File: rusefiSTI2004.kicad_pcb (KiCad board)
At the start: 4 copper layers, 138.6 x 113.6 mm, 137 parts, among them J1 TE_1-1376430-0, J2 USB C 2.0 16P, J3 Molex_39281143, M1 Module-mega-mcu144-0.7, M10 Module-lin-0.1, M11 Module-dinput4-0.1, M12 Module-dinput4-0.1, M13 Module-knock-0.2, M14 Module-power_12and5V-0.3, M2 Module-motor-driver-0.1, M3 Module-wbo-0.5, M5 Module-vr-discrete-0.5, M8 Module-power_12and5V-0.3, M9 Module-motor-driver-0.1, P1 WBO_UN, P10 OUT_SPARE_LS2, P11 CHARGE_A22, P12 FP_STATUS, P13 DLC6_D29, P14 SPARE_IGN6, P15 SPARE_IGN7, P16 SPARE_IGN8, P17 I2C_1_SCL, P18 I2C_1_SDA, P19 +5VA, P2 WBO_VM, P20 +3.3V, P21 +12V_RAW, P22 GND, P23 BOOT0, P24 SWDIO, P25 SWCLK, P26 NRST, P27 SPARE_PWM3, P28 SPARE_RES2, P29 AUX_IN1, P3 WBO_IP, P30 AUX_IN2, P31 AUX_IN3, P32 PG_5VP_APS, P4 WBO_RTRIM, P5 WBO_HEATER, P6 CAN_H, P7 CAN_L, P8 K_LINE, P9 OUT_SPARE_LS1, Q1 NCV8401BDTRKG, Q10 NCV8401BDTRKG, Q11 NCV8401BDTRKG, Q12 NCV8401BDTRKG, Q13 ZXMS6006DGQ-13, Q14 ZXMS6006DGQ-13, Q15 ZXMS6006DGQ-13, Q16 ZXMS6006DGQ-13, Q17 ZXMS6004FFTA, Q18 ZXMS6004FFTA, Q19 ZXMS6004FFTA, Q2 NCV8401BDTRKG, Q20 ZXMS6004FFTA, Q3 NCV8401BDTRKG, Q4 NCV8401BDTRKG, Q5 ZXMS6004FFTA, Q6 ZXMS6004FFTA, Q7 ZXMS6004FFTA, Q8 ZXMS6004FFTA, Q9 NCV8401BDTRKG, U1 USBLC6-2SC6

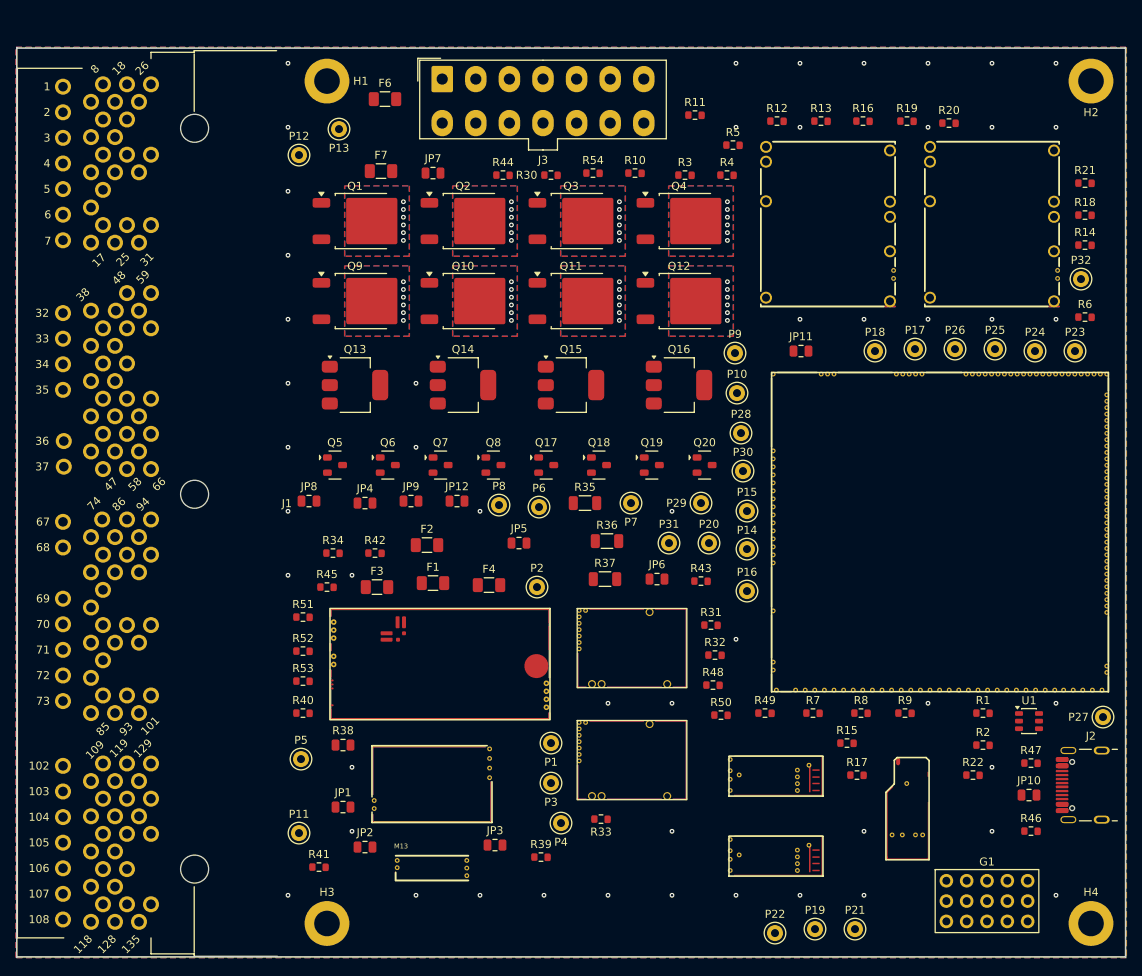
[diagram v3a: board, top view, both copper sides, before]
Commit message: Low-side drivers as on the newest rusEFI boards: 10 x VNLD5160 dual SO-8 + 1 NCV8401B DPAK for the rear O2 heater
rusEFI uaefi-f, hellen-112-17 and hellen154hyundai-e use VNLD5090/VNLD5160 for general outputs and
keep one DPAK for the heaviest load; our Hellen modules already carry their other ICs. Every output
keeps its J1 and MCU pin (netlist checked); U19B parked as a spare. PCB re-placed: DRC 0 errors.

Co-Authored-By: Claude Opus 5.5 <noreply@anthropic.com>
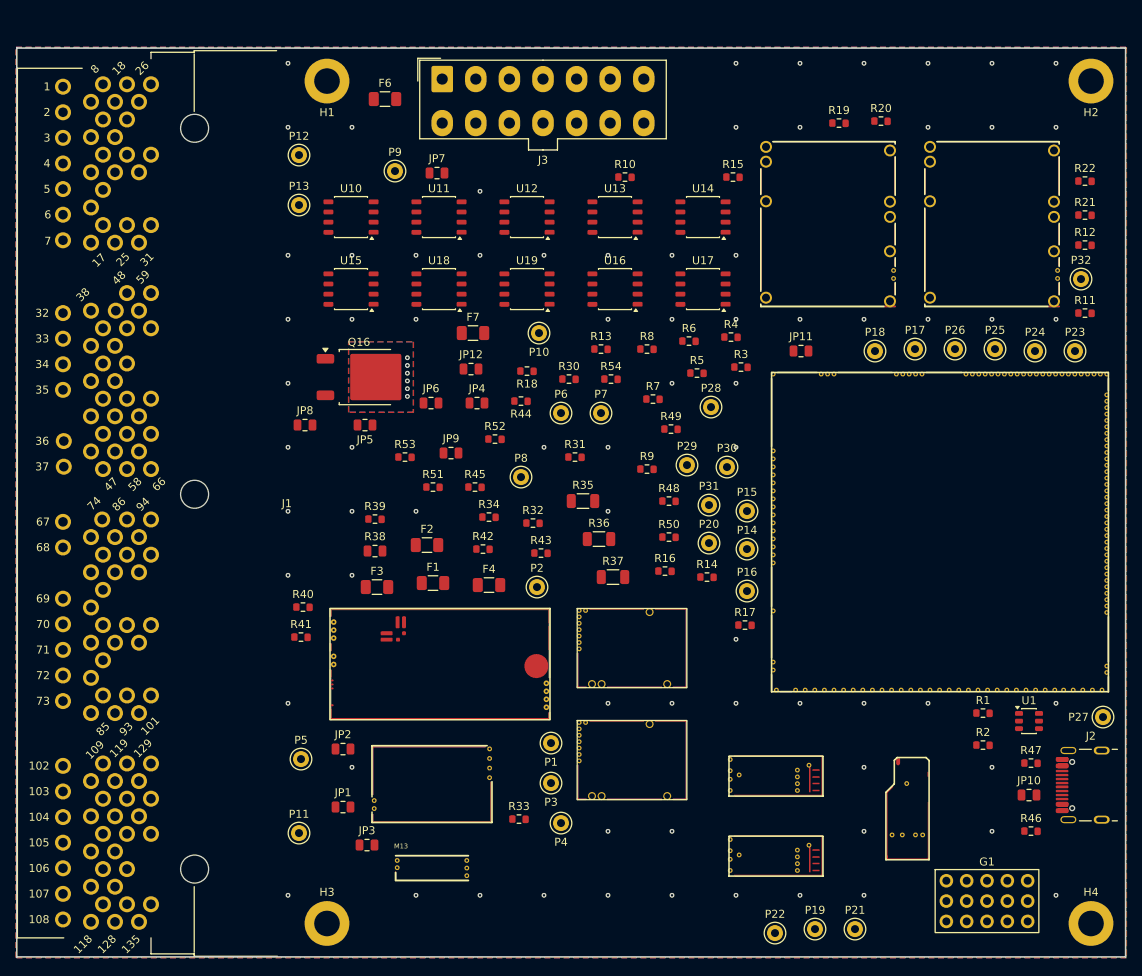
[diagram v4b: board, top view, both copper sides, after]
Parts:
- removed Q1, Q10, Q11, Q12, Q2, Q3, Q4, Q9: NCV8401BDTRKG, EmbeddedEra_Library:TO-252-2
- removed Q13, Q14, Q15: ZXMS6006DGQ-13, EmbeddedEra_Library:SOT-223-3_TabPin2
- removed Q17, Q18, Q19, Q20, Q5, Q6, Q7, Q8: ZXMS6004FFTA, EmbeddedEra_Library:SOT-23F_Diodes
- added U10: VNLD5160TR-E, EmbeddedEra_Library:SOIC-8_3.9x4.9mm_P1.27mm, F.Cu at (127.0, 57.0)
- added U11: VNLD5160TR-E, EmbeddedEra_Library:SOIC-8_3.9x4.9mm_P1.27mm, F.Cu at (138.0, 57.0)
- added U12: VNLD5160TR-E, EmbeddedEra_Library:SOIC-8_3.9x4.9mm_P1.27mm, F.Cu at (149.0, 57.0)
- added U13: VNLD5160TR-E, EmbeddedEra_Library:SOIC-8_3.9x4.9mm_P1.27mm, F.Cu at (160.0, 57.0)
- added U14: VNLD5160TR-E, EmbeddedEra_Library:SOIC-8_3.9x4.9mm_P1.27mm, F.Cu at (171.0, 57.0)
- added U15: VNLD5160TR-E, EmbeddedEra_Library:SOIC-8_3.9x4.9mm_P1.27mm, F.Cu at (127.0, 66.0)
- added U16: VNLD5160TR-E, EmbeddedEra_Library:SOIC-8_3.9x4.9mm_P1.27mm, F.Cu at (160.0, 66.0)
- added U17: VNLD5160TR-E, EmbeddedEra_Library:SOIC-8_3.9x4.9mm_P1.27mm, F.Cu at (171.0, 66.0)
- added U18: VNLD5160TR-E, EmbeddedEra_Library:SOIC-8_3.9x4.9mm_P1.27mm, F.Cu at (138.0, 66.0)
- added U19: VNLD5160TR-E, EmbeddedEra_Library:SOIC-8_3.9x4.9mm_P1.27mm, F.Cu at (149.0, 66.0)
- Q16: value ZXMS6006DGQ-13 -> NCV8401BDTRKG; footprint EmbeddedEra_Library:SOT-223-3_TabPin2 -> EmbeddedEra_Library:TO-252-2
- moved R22 75.6 mm to (218.8, 52.5)
- moved R18 72.4 mm to (149.0, 76.2)
- moved R15 72.2 mm to (174.8, 52.0)
- moved R14 62.9 mm to (171.5, 102.0)
- moved R16 61.5 mm to (166.2, 101.2)
- moved R11 54.7 mm to (218.8, 69.0)
- moved R8 52.8 mm to (164.0, 73.5)
- moved R6 49.6 mm to (169.2, 72.5)
- moved P9 48.2 mm to (132.5, 51.2)
- moved R39 47.1 mm to (130.0, 94.8)
- moved R9 44.4 mm to (164.0, 88.5)
- moved R7 44.1 mm to (164.8, 79.8)
- moved R12 41.5 mm to (218.8, 60.5)
- moved R13 39.6 mm to (158.2, 73.5)
- moved Q16 39.2 mm to (128.8, 77.0)
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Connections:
- Q16 pad 1: SPARE_LS2 -> O2_HEATER_REAR
- Q16 pad 2: OUT_SPARE_LS2 -> OUT_O2_HEATER_REAR
- R14 pad 1: O2_HEATER_REAR -> PURGE
- R15 pad 1: PURGE -> AC_RELAY
- R16 pad 1: AC_RELAY -> SPARE_LS1
- R17 pad 1: SPARE_LS1 -> SPARE_LS2
- R18 pad 1: SPARE_LS2 -> O2_HEATER_REAR
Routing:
- net OUT_WG: vias 6 -> 0
- net OUT_VVT_RH-: vias 6 -> 0
- net OUT_VVT_LH-: vias 6 -> 0
- net OUT_INJ4: vias 6 -> 0
- net OUT_INJ3: vias 6 -> 0
- net OUT_INJ2: vias 6 -> 0
- net OUT_INJ1: vias 6 -> 0
- net GND: vias 51 -> 74
- removed copper zone on B.Cu, net OUT_INJ1
- removed copper zone on F.Cu, net OUT_INJ1
- removed copper zone on B.Cu, net OUT_INJ2
- removed copper zone on F.Cu, net OUT_INJ2
- removed copper zone on B.Cu, net OUT_INJ3
- removed copper zone on F.Cu, net OUT_INJ3
- removed copper zone on B.Cu, net OUT_INJ4
- removed copper zone on F.Cu, net OUT_INJ4
- removed copper zone on B.Cu, net OUT_VVT_LH-
- removed copper zone on F.Cu, net OUT_VVT_LH-
- removed copper zone on B.Cu, net OUT_VVT_RH-
- removed copper zone on F.Cu, net OUT_VVT_RH-
- removed copper zone on B.Cu, net OUT_WG
- removed copper zone on F.Cu, net OUT_WG

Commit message: PCB: pull-ups/downs and fuses next to the pin they serve
Gate pull-downs at their VNLD5160/DPAK input pins, switch-input pulls in a column beside J1 at
their pin, USB CC resistors at J2, coil PTCs at J1, aux fuses at J3. Driver bank 4x3 to free the
column. DRC 0 errors, parity 0.

Co-Authored-By: Claude Opus 5.5 <noreply@anthropic.com>
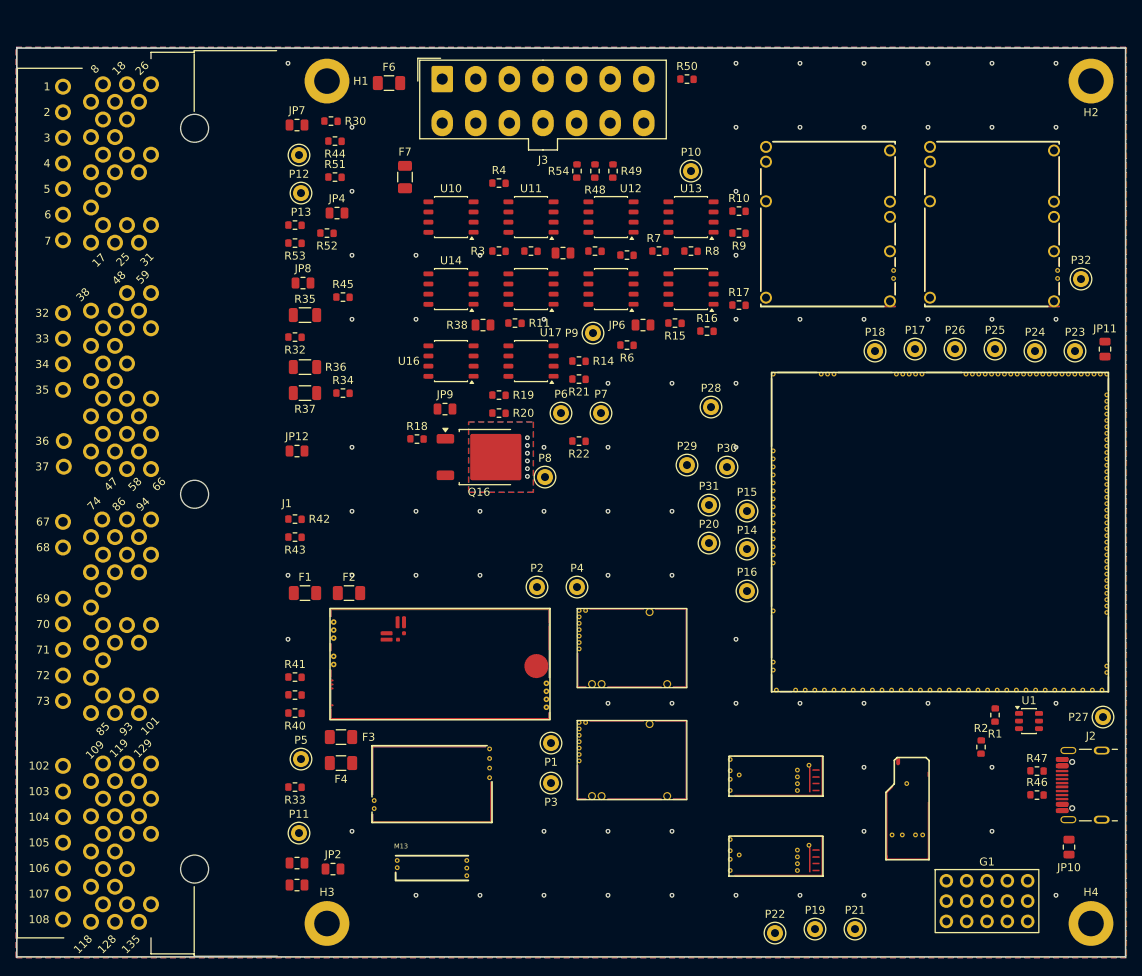
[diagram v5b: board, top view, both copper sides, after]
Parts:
- moved R11 71.3 mm to (147.5, 70.2)
- moved R22 71.1 mm to (155.5, 85.0)
- moved R12 69.3 mm to (149.5, 61.2)
- moved R21 66.5 mm to (155.5, 77.2)
- moved R20 60.1 mm to (145.5, 81.5)
- moved R50 57.3 mm to (169.0, 39.8)
- moved R19 54.4 mm to (145.5, 79.2)
- moved R31 45.5 mm to (120.0, 58.0)
- moved R37 44.8 mm to (121.2, 79.0)
- moved R30 43.9 mm to (124.5, 45.0)
- moved R36 42.6 mm to (121.2, 75.8)
- moved R48 42.3 mm to (157.5, 51.2), turned to -90 degrees
- moved R35 41.8 mm to (121.2, 69.2)
- moved R51 40.6 mm to (125.0, 52.0)
- moved R17 40.0 mm to (175.5, 68.0)
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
